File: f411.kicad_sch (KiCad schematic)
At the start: 3 parts, among them J9 Conn_02x04_Top_Bottom, U3 f411-RFM95W

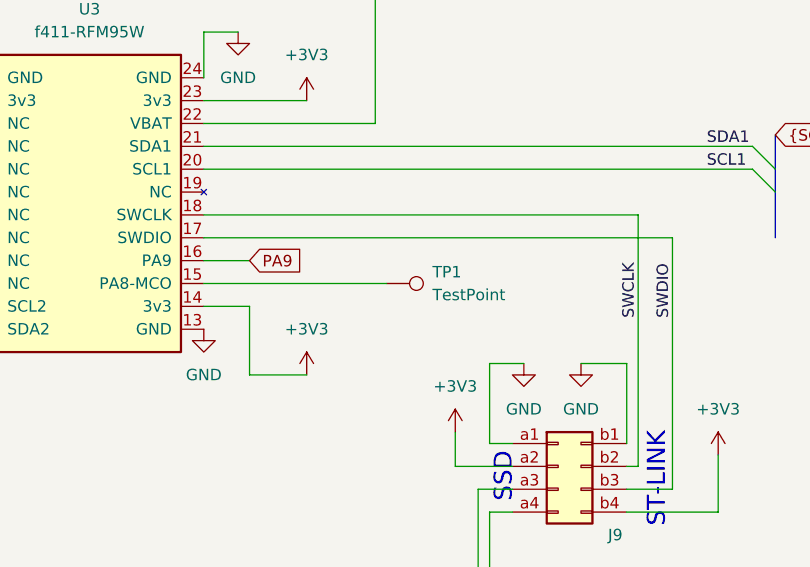
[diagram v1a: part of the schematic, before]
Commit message: 3d showing well with MCU-LoRa step model. Clean up of silkscreen and fab layers. Small movement of some components so silkscreen label placement is better.
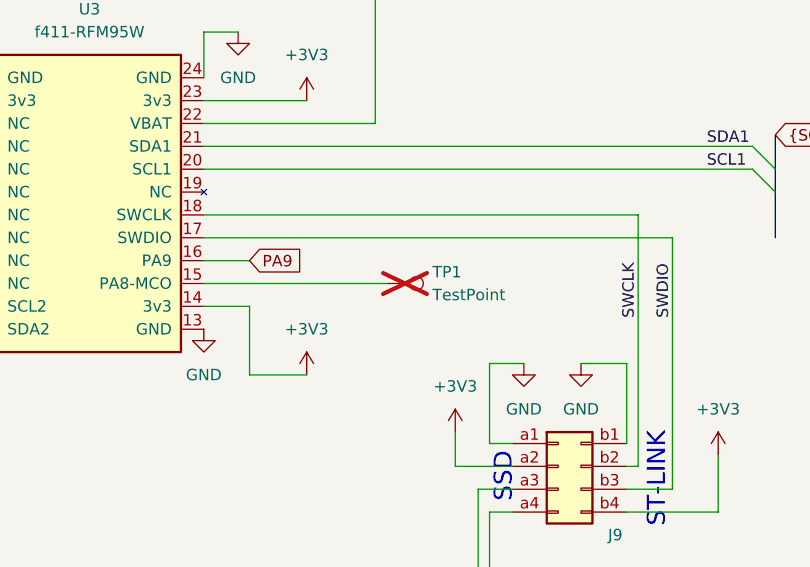
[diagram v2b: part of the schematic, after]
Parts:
- TP1: now not fitted; now left out of the parts list
- U3: now left out of the parts list
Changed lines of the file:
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@@
 		(unit 1)
 		(exclude_from_sim no)
-		(in_bom yes)
+		(in_bom no)
 		(on_board yes)
 		(dnp no)
@@
 		(unit 1)
 		(exclude_from_sim no)
-		(in_bom yes)
+		(in_bom no)
 		(on_board yes)
-		(dnp no)
+		(dnp yes)
 		(fields_autoplaced yes)
 		(property "Reference" "TP1"

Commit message: ongoing.
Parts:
- removed TP1: TestPoint, ProjectLib:TestPoint_Pad_D1.0mm, symbol MySymbols:TestPoint
- removed U3: f411-RFM95W, ProjectLib:Castellated_MCU-LoRa_20x50mm_2x12_P2.0mm_SMD, symbol MySymbol_Library:f411-RFM95
- added C?: 4.7µF, ProjectLib:C_0402_1005Metric, symbol ProjectLib:C
- added C? (x2): 100nF, ProjectLib:C_0402_1005Metric, symbol ProjectLib:C
- added D?: blue 2ma 2.65Vf, ProjectLib:LED_0603_1608Metric, symbol ProjectLib:LED
- added D?: red 2ma 1.8Vf, ProjectLib:LED_0603_1608Metric, symbol ProjectLib:LED
- added L?: 2.2uH, ProjectLib:L_0402_1005Metric, symbol ProjectLib:L
- added R? (x5): 10k 1%, ProjectLib:R_0402_1005Metric, symbol ProjectLib:R_US
- added R?: 280 1%, ProjectLib:R_0402_1005Metric, symbol ProjectLib:R_US
- added R?: 715 1%, ProjectLib:R_0402_1005Metric, symbol ProjectLib:R_US
- added SW? (x2): SW_Push, ProjectLib:SW_SPST_B3U-1000P, symbol ProjectLib:SW_Push
- added TP?: MCO, ProjectLib:TestPoint_Pad_D1.0mm, symbol ProjectLib:Conn_01x01_Socket
- added TP?: BT1 b2, ProjectLib:TestPoint_Pad_D1.0mm, symbol ProjectLib:TestPoint
- added U?: STM32F411CEU6, ProjectLib:QFN-48-1EP_7x7mm_P0.5mm_EP5.6x5.6mm, symbol ProjectLib:STM32F411CEUx
- J?: renamed from J9; MfgPart HC-PM254-5.0H-2x8PS -> HC-PM254-5.0H-2x4PS-02A
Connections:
- net +3V3: now also D?.2 (A), L?.2, R?.1, R?.1, R?.1, R?.2, SW?.1, U?.24 (VDD), U?.36 (VDD), U?.48 (VDD)
- net GND: now also C?.1, C?.2, C?.2, R?.2, R?.2, R?.2, SW?.1, U?.23 (VSS), U?.35 (VSS), U?.47 (VSS), U?.49 (VSS), U?.8 (VSSA)
- net SCL1: now also R?.2, U?.45 (PB8)
- net SCL2: now also U?.21 (PB10)
- net SDA1: now also R?.1, U?.46 (PB9)
- net SDA2: now also U?.39 (PB3)
- net SWCLK: now also U?.37 (PA14)
- net SWDIO: now also U?.34 (PA13)
- net VBAT: now also U?.1 (VBAT)
- new net: R?.1, SW?.2, U?.44 (BOOT0)
- new net: TP?.1 (Pin_1), U?.29 (PA8)
- new net: C?.1, U?.22 (VCAP1)
- new net: D?.1 (K), U?.2 (PC13)
- new net: D?.2 (A), R?.2
- new net: R?.1, TP?.1, U?.20 (PB2)
- new net: C?.2, R?.2, SW?.2, U?.7 (NRST)
- new net: C?.1, L?.1, U?.9 (VDDA/VREF+)
- new net: D?.1 (K), R?.1
- new net DIO0: U?.40 (PB4)
- new net DIO1: U?.41 (PB5)
- new net MISO: U?.16 (PA6)
- new net MOSI: U?.17 (PA7)
- new net NSS: U?.14 (PA4)
- new net PC14_OSC32_IN: U?.3 (PC14)
- new net PC15_OSC32_OUT: U?.4 (PC15)
- new net PH0_OSC_IN: U?.5 (PH0)
- new net PH1_OSC_OUT: U?.6 (PH1)
- new net RESET: U?.11 (PA1)
- new net SCK: U?.15 (PA5)
- no-connect marks 0 -> 16
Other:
- added sheet HSE (HSE.kicad_sch)
- added sheet LSE (LSE.kicad_sch)
- added sheet RFM95W (RFM95W.kicad_sch)
- title: Multiplex I2C to Screw Terminal connectors -> stm32f411, ST-Link & SSD
- moved on the sheet: J?

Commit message: ongoing.
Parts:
- gave numbers to parts that had none: 19

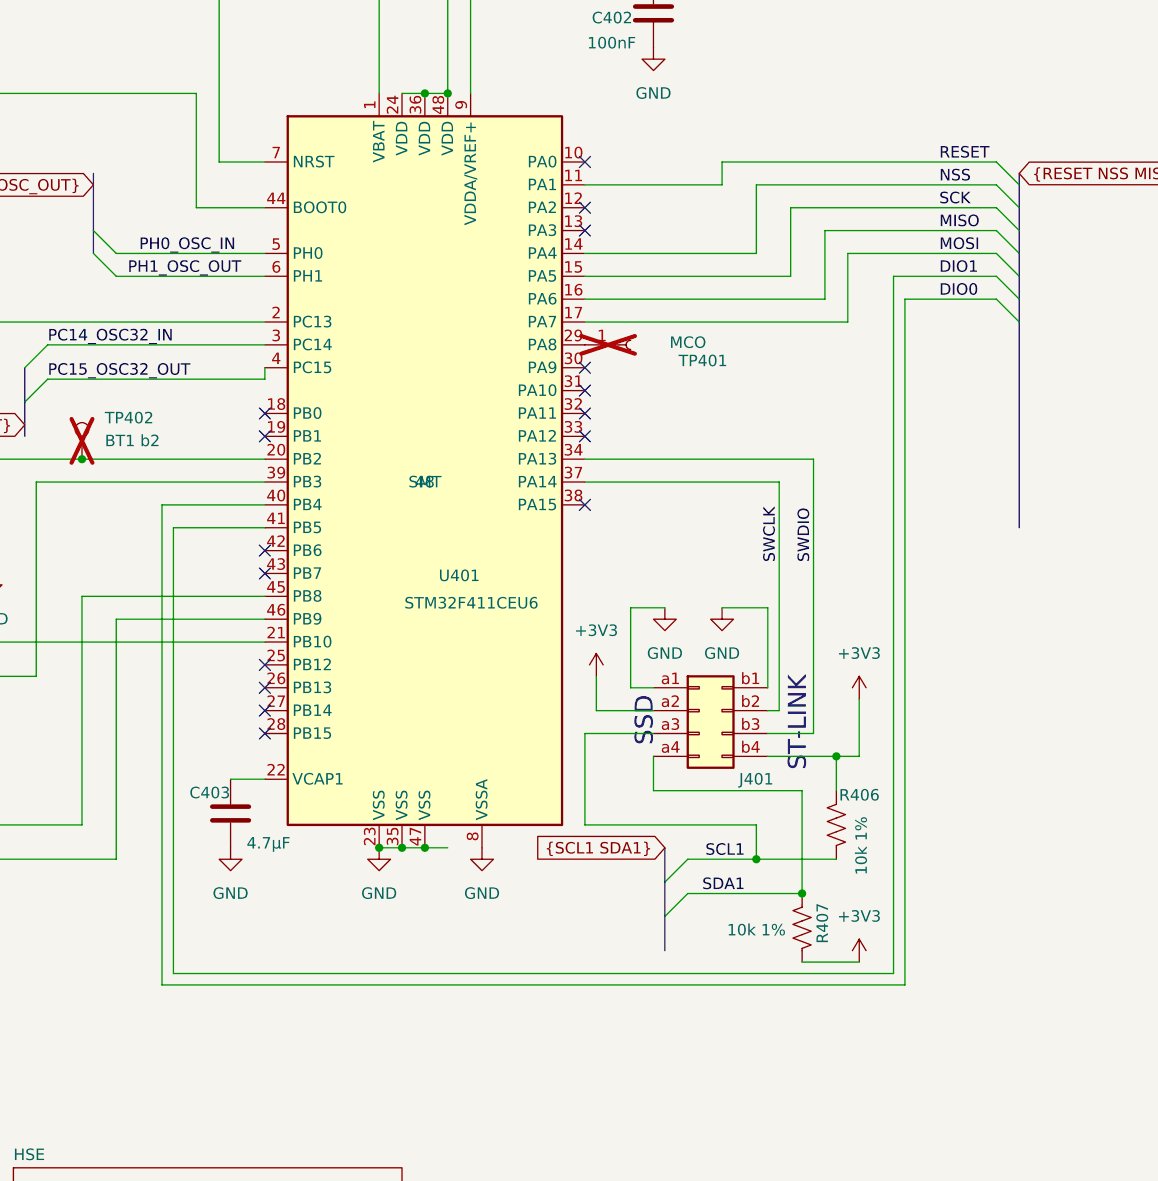
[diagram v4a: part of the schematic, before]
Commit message: schematic good. Footprint placement ongoing.
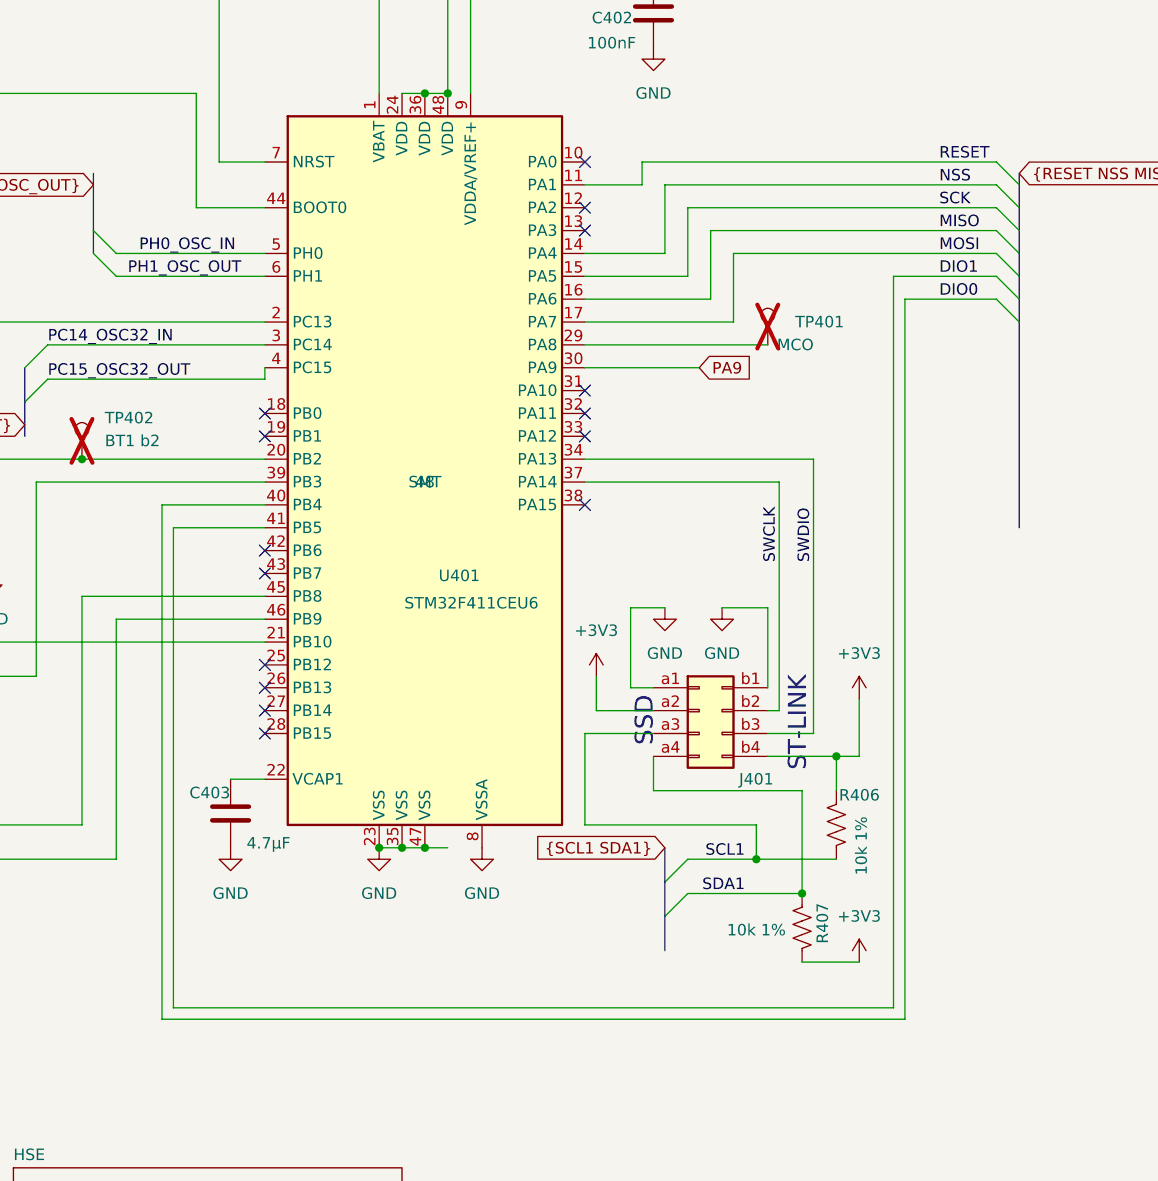
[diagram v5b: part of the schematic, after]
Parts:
- TP401: symbol ProjectLib:Conn_01x01_Socket -> ProjectLib:TestPoint; now in the parts list
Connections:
- net PA9: now reaches U401.30 (PA9)
- no-connect marks 16 -> 15
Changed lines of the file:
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@@
 	(title_block
 		(title "stm32f411, ST-Link & SSD")
-		(date "2025-09-15")
-		(rev "v0.2.2")
+		(date "2025-11-30")
+		(rev "v0.2.3")
 	)
 	(text "SSD"
@@
 	)
 	(no_connect
-		(at 162.56 90.17)
-	)
-	(no_connect
 		(at 127 130.81)
 	)
@@
 	(wire
 		(pts
-			(xy 185.42 80.01) (xy 185.42 72.39)
+			(xy 173.99 80.01) (xy 173.99 72.39)
 		)
 		(stroke
@@
 	(wire
 		(pts
-			(xy 162.56 82.55) (xy 189.23 82.55)
+			(xy 162.56 82.55) (xy 176.53 82.55)
 		)
 		(stroke
@@
 	(wire
 		(pts
-			(xy 196.85 157.48) (xy 196.85 80.01)
+			(xy 196.85 161.29) (xy 196.85 80.01)
 		)
 		(stroke
@@
 	(wire
 		(pts
-			(xy 162.56 80.01) (xy 185.42 80.01)
+			(xy 162.56 80.01) (xy 173.99 80.01)
 		)
 		(stroke
@@
 	(wire
 		(pts
-			(xy 189.23 82.55) (xy 189.23 74.93)
+			(xy 176.53 82.55) (xy 176.53 74.93)
 		)
 		(stroke
@@
 	(wire
 		(pts
-			(xy 191.77 85.09) (xy 191.77 77.47)
+			(xy 179.07 85.09) (xy 179.07 77.47)
 		)
 		(stroke
@@
 	(wire
 		(pts
-			(xy 162.56 85.09) (xy 191.77 85.09)
+			(xy 162.56 85.09) (xy 179.07 85.09)
 		)
 		(stroke
@@
 	(wire
 		(pts
-			(xy 116.84 107.95) (xy 116.84 157.48)
+			(xy 116.84 107.95) (xy 116.84 161.29)
 		)
 		(stroke
@@
 	(wire
 		(pts
-			(xy 198.12 82.55) (xy 198.12 158.75)
+			(xy 198.12 82.55) (xy 198.12 162.56)
 		)
 		(stroke
@@
 	(wire
 		(pts
-			(xy 162.56 77.47) (xy 181.61 77.47)
+			(xy 162.56 77.47) (xy 171.45 77.47)
 		)
 		(stroke
@@
 	(wire
 		(pts
-			(xy 181.61 77.47) (xy 181.61 69.85)
+			(xy 171.45 77.47) (xy 171.45 69.85)
 		)
 		(stroke
@@
 	(wire
 		(pts
+			(xy 162.56 87.63) (xy 182.88 87.63)
+		)
+		(stroke
+			(width 0)
+			(type default)
+		)
+	)
+	(wire
+		(pts
 			(xy 101.6 102.87) (xy 101.6 124.46)
 		)
@@
 	(wire
 		(pts
-			(xy 191.77 77.47) (xy 208.28 77.47)
+			(xy 179.07 77.47) (xy 208.28 77.47)
 		)
 		(stroke
@@
 	(wire
 		(pts
-			(xy 162.56 69.85) (xy 177.8 69.85)
+			(xy 162.56 69.85) (xy 168.91 69.85)
 		)
 		(stroke
@@
 	(wire
 		(pts
-			(xy 116.84 157.48) (xy 196.85 157.48)
+			(xy 116.84 161.29) (xy 196.85 161.29)
+		)
+		(stroke
+			(width 0)
+			(type default)
+		)
+	)
+	(wire
+		(pts
+			(xy 162.56 90.17) (xy 175.26 90.17)
 		)
 		(stroke
@@
 	(wire
 		(pts
-			(xy 198.12 158.75) (xy 115.57 158.75)
+			(xy 198.12 162.56) (xy 115.57 162.56)
 		)
 		(stroke
@@
 	(wire
 		(pts
-			(xy 115.57 105.41) (xy 115.57 158.75)
+			(xy 115.57 105.41) (xy 115.57 162.56)
 		)
 		(stroke
@@
 	(wire
 		(pts
-			(xy 181.61 69.85) (xy 208.28 69.85)
+			(xy 171.45 69.85) (xy 208.28 69.85)
 		)
 		(stroke
@@
 	(wire
 		(pts
-			(xy 185.42 72.39) (xy 208.28 72.39)
+			(xy 173.99 72.39) (xy 208.28 72.39)
 		)
 		(stroke
@@
 	(wire
 		(pts
-			(xy 189.23 74.93) (xy 208.28 74.93)
+			(xy 176.53 74.93) (xy 208.28 74.93)
 		)
 		(stroke
@@
 	(wire
 		(pts
-			(xy 177.8 67.31) (xy 177.8 69.85)
+			(xy 168.91 67.31) (xy 168.91 69.85)
 		)
 		(stroke
@@
 	(wire
 		(pts
-			(xy 177.8 67.31) (xy 208.28 67.31)
+			(xy 168.91 67.31) (xy 208.28 67.31)
 		)
 		(stroke
@@
 		)
 	)
+	(global_label "PA9"
+		(shape input)
+		(at 175.26 90.17 0)
+		(fields_autoplaced yes)
+		(effects
+			(font
+				(size 1.27 1.27)
+			)
+			(justify left)
+		)
+		(property "Intersheetrefs" "${INTERSHEET_REFS}"
+			(at 181.8133 90.17 0)
+			(effects
+				(font
+					(size 1.27 1.27)
+				)
+				(justify left)
+				(hide yes)
+			)
+		)
+	)
 	(global_label "{RESET NSS MISO MOSI SCK DIO0 DIO1}"
 		(shape input)
@@
 			)
 		)
-		(property "Datasheet" ""
+		(property "Datasheet" "~"
 			(at 64.77 63.5 0)
 			(effects
@@
 			)
 		)
-		(property "Datasheet" ""
+		(property "Datasheet" "~"
 			(at 186.69 152.4 0)
 			(effects
@@
 	)
 	(symbol
-		(lib_id "ProjectLib:Conn_01x01_Socket")
-		(at 167.64 87.63 0)
+		(lib_id "ProjectLib:TestPoint")
+		(at 182.88 87.63 0)
 		(unit 1)
 		(exclude_from_sim no)
-		(in_bom no)
+		(in_bom yes)
 		(on_board yes)
 		(dnp yes)
 		(property "Reference" "TP401"
-			(at 172.974 89.408 0)
+			(at 185.928 85.09 0)
 			(effects
 				(font
@@
 		)
 		(property "Value" "MCO"
-			(at 171.958 87.376 0)
+			(at 183.896 87.63 0)
 			(effects
 				(font
@@
 		)
 		(property "Footprint" "ProjectLib:TestPoint_Pad_D1.0mm"
-			(at 167.64 87.63 0)
+			(at 187.96 87.63 0)
 			(effects
 				(font
@@
 		)
 		(property "Datasheet" "~"
-			(at 167.64 87.63 0)
+			(at 187.96 87.63 0)
 			(effects
 				(font
@@
 			)
 		)
-		(property "Description" "Generic connector, single row, 01x01, script generated"
-			(at 167.64 87.63 0)
+		(property "Description" "test point"
+			(at 182.88 87.63 0)
 			(effects
 				(font
@@
 		)
 		(property "MountType" "PTH"
-			(at 167.64 87.63 0)
+			(at 182.88 87.63 0)
 			(effects
 				(font
@@
 		)
 		(property "pads" ""
-			(at 167.64 87.63 0)
+			(at 182.88 87.63 0)
 			(effects
 				(font
@@
 		)
 		(property "Package" ""
-			(at 167.64 87.63 0)
+			(at 182.88 87.63 0)
 			(effects
 				(font
@@
 		)
 		(property "Note" ""
-			(at 167.64 87.63 0)
+			(at 182.88 87.63 0)
 			(effects
 				(font
@@
 			)
 		)
-		(property "Datasheet" ""
+		(property "Datasheet" "~"
 			(at 123.19 139.7 0)
 			(effects
@@
 			)
 		)
-		(property "Datasheet" "https://www.kingbrightusa.com/images/catalog/SPEC/APT1608LVBC-D.pdf"
+		(property "Datasheet" "~"
 			(at 69.85 85.09 0)
 			(effects
@@
 			)
 		)
-		(property "Datasheet" ""
+		(property "Datasheet" "~"
 			(at 96.52 109.22 0)
 			(effects
@@
 			)
 		)
-		(property "Datasheet" "https://www.lcsc.com/product-detail/C42163132.html"
+		(property "Datasheet" "~"
 			(at 175.26 128.27 0)
 			(effects
@@
 			)
 		)
-		(property "Description" "PinSocket  02x04 connector, low profile"
+		(property "Description" "Generic connector, double row, 02x04, row letter first pin numbering scheme (pin number consists of a letter for the row and a number for the pin index in this row. a1, ..., aN; b1, ..., bN), script generated (kicad-library-utils/schlib/autogen/connector/)"
 			(at 175.26 128.27 0)
 			(effects
@@
 			)
 		)
-		(property "Datasheet" ""
+		(property "Datasheet" "~"
 			(at 67.31 44.45 0)
 			(effects
@@
 			)
 		)
-		(property "Datasheet" ""
+		(property "Datasheet" "~"
 			(at 58.42 54.61 0)
 			(effects
@@
 			)
 		)
-		(property "Datasheet" ""
+		(property "Datasheet" "~"
 			(at 170.18 50.8 0)
 			(effects
@@
 			)
 		)
-		(property "Datasheet" ""
+		(property "Datasheet" "~"
 			(at 71.12 34.29 0)
 			(effects
@@
 			)
 		)
-		(property "Datasheet" "https://product.tdk.com/en/system/files?file=dam/doc/product/inductor/inductor/smd/catalog/inductor_commercial_decoupling_mlz1005_en.pdf"
+		(property "Datasheet" "~"
 			(at 170.18 43.18 0)
 			(effects
@@
 			)
 		)
-		(property "Datasheet" "https://www.kingbrightusa.com/images/catalog/SPEC/APT1608LSECK-J3-PRV.pdf"
+		(property "Datasheet" "~"
 			(at 41.91 72.39 0)
 			(effects
@@
 			)
 		)
-		(property "Datasheet" ""
+		(property "Datasheet" "~"
 			(at 93.98 40.64 0)
 			(effects
@@
 			)
 		)
-		(property "Datasheet" ""
+		(property "Datasheet" "~"
 			(at 190.5 140.97 0)
 			(effects
@@
 			)
 		)
-		(property "Datasheet" ""
+		(property "Datasheet" "~"
 			(at 62.23 85.09 0)
 			(effects
@@
 			)
 		)
-		(property "Datasheet" ""
+		(property "Datasheet" "~"
 			(at 41.91 80.01 0)
 			(effects

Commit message: ERC and DRC good. Needs fab layer cleanup.
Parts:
- added R408, R409: 10k 1%, ProjectLib:R_0402_1005Metric, symbol ProjectLib:R_US
- SW401: value SW_Push -> RST
- SW402: value SW_Push -> BT0
- TP402: value BT1 b2 -> BT1
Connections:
- net +3V3: now also R408.1, R409.1
- net SCL2: now also R408.2
- net SDA2: now also R409.2
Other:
- moved on the sheet: R405

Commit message: ongoing.
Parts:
- SW401: value RST -> SW_Push; label (none) -> RST
- SW402: value BT0 -> SW_Push; label (none) -> BT0
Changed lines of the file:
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@@
 			)
 		)
-		(property "Datasheet" ""
+		(property "Datasheet" "https://www.kingbrightusa.com/images/catalog/SPEC/APT1608LVBC-D.pdf"
 			(at 69.85 85.09 0)
 			(effects
@@
 		(dnp no)
 		(property "Reference" "C401"
-			(at 70.104 42.418 90)
+			(at 71.628 42.418 90)
 			(effects
 				(font
@@
 			)
 		)
-		(property "Value" "BT0"
+		(property "Value" "SW_Push"
 			(at 58.42 54.61 0)
 			(effects
@@
 					(size 1.27 1.27)
 				)
+				(hide yes)
 			)
 		)
@@
 			)
 		)
-		(property "Datasheet" "~"
+		(property "Datasheet" "https://omronfs.omron.com/en_US/ecb/products/pdf/en-b3u.pdf"
 			(at 58.42 54.61 0)
 			(effects
@@
 			)
 		)
-		(property "Note" ""
-			(at 58.42 59.69 0)
-			(effects
-				(font
-					(size 1.27 1.27)
-				)
-				(hide yes)
+		(property "label" "BT0"
+			(at 58.166 55.372 0)
+			(effects
+				(font
+					(size 1.27 1.27)
+				)
 			)
 		)
@@
 			)
 		)
-		(property "Value" "RST"
+		(property "Value" "SW_Push"
 			(at 71.12 34.29 0)
 			(effects
@@
 					(size 1.27 1.27)
 				)
+				(hide yes)
 			)
 		)
@@
 			)
 		)
-		(property "Datasheet" "~"
+		(property "Datasheet" "https://omronfs.omron.com/en_US/ecb/products/pdf/en-b3u.pdf"
 			(at 71.12 34.29 0)
 			(effects
@@
 			)
 		)
-		(property "Note" ""
-			(at 71.12 39.37 0)
-			(effects
-				(font
-					(size 1.27 1.27)
-				)
-				(hide yes)
+		(property "label" "RST"
+			(at 70.612 34.29 0)
+			(effects
+				(font
+					(size 1.27 1.27)
+				)
 			)
 		)
@@
 			)
 		)
-		(property "Datasheet" "~"
+		(property "Datasheet" "https://product.tdk.com/en/system/files?file=dam/doc/product/inductor/inductor/smd/catalog/inductor_commercial_decoupling_mlz1005_en.pdf"
 			(at 170.18 43.18 0)
 			(effects
@@
 			)
 		)
-		(property "Datasheet" ""
+		(property "Datasheet" "https://www.kingbrightusa.com/images/catalog/SPEC/APT1608LSECK-J3-PRV.pdf"
 			(at 41.91 72.39 0)
 			(effects
